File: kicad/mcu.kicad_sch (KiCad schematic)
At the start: 3 parts, among them J8 Conn_01x04, U5 ESP32-C6-DEVKITC-1-N8

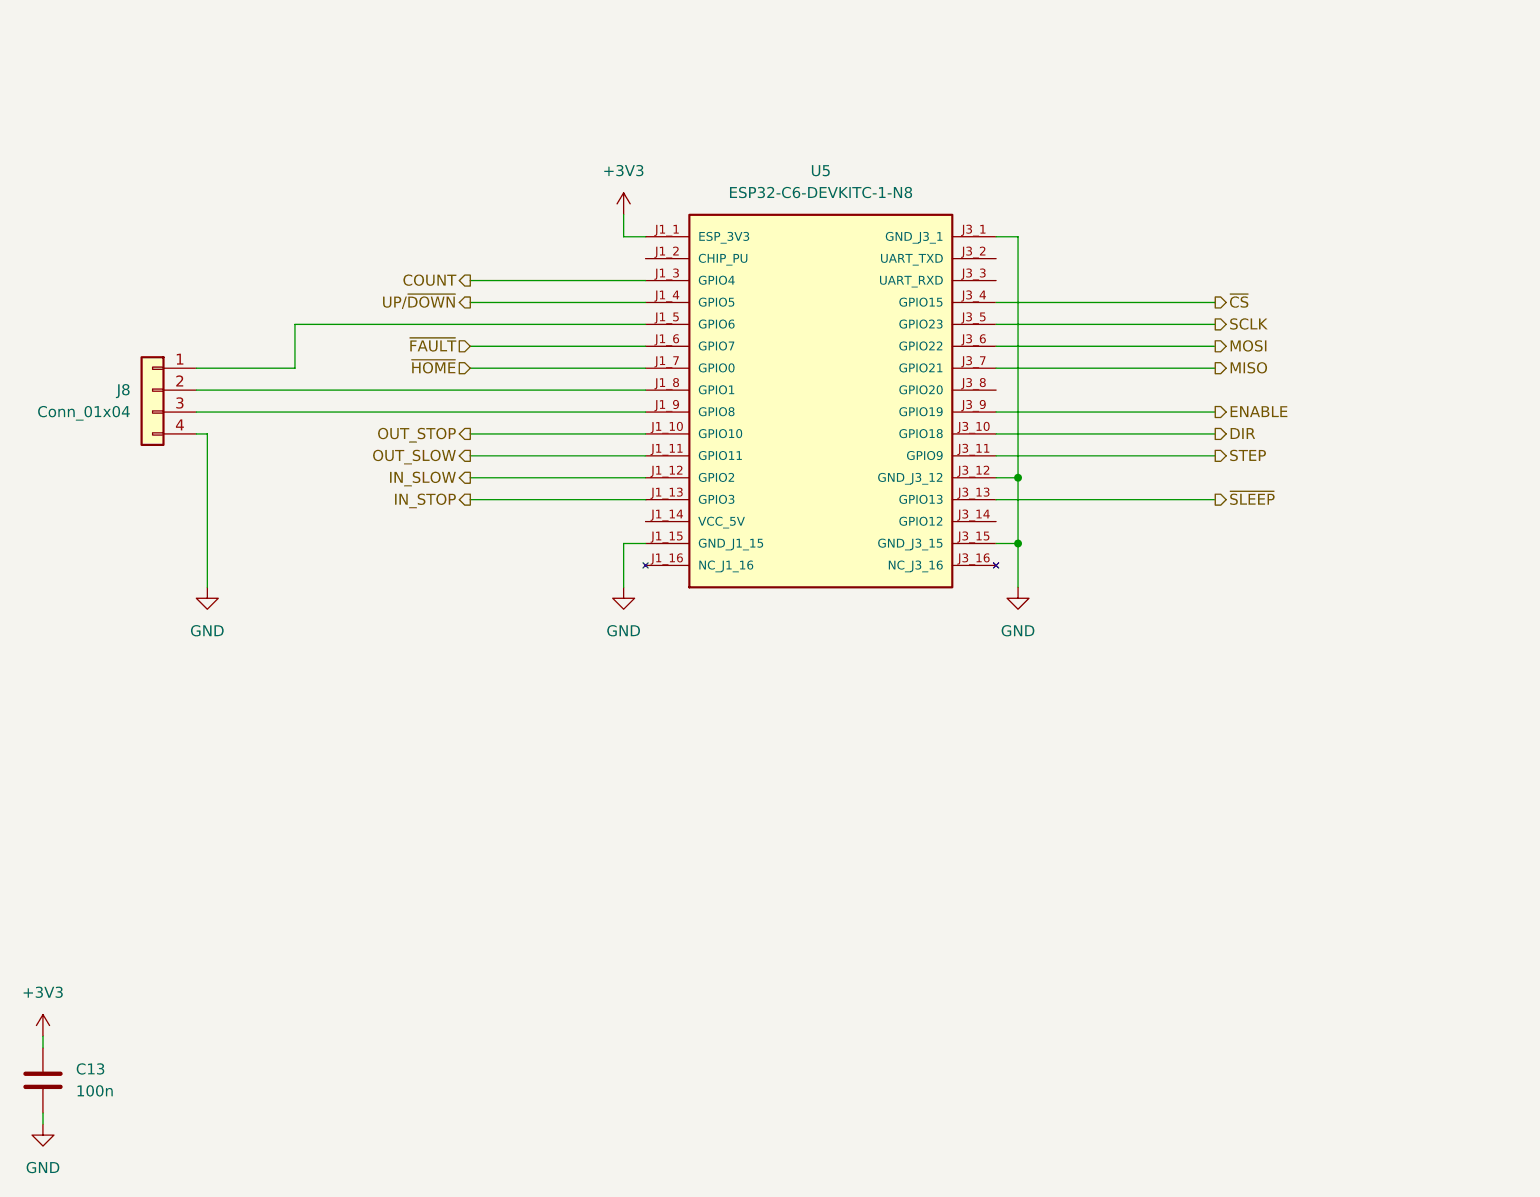
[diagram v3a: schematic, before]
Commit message: Finished the schematic and started the PCB.
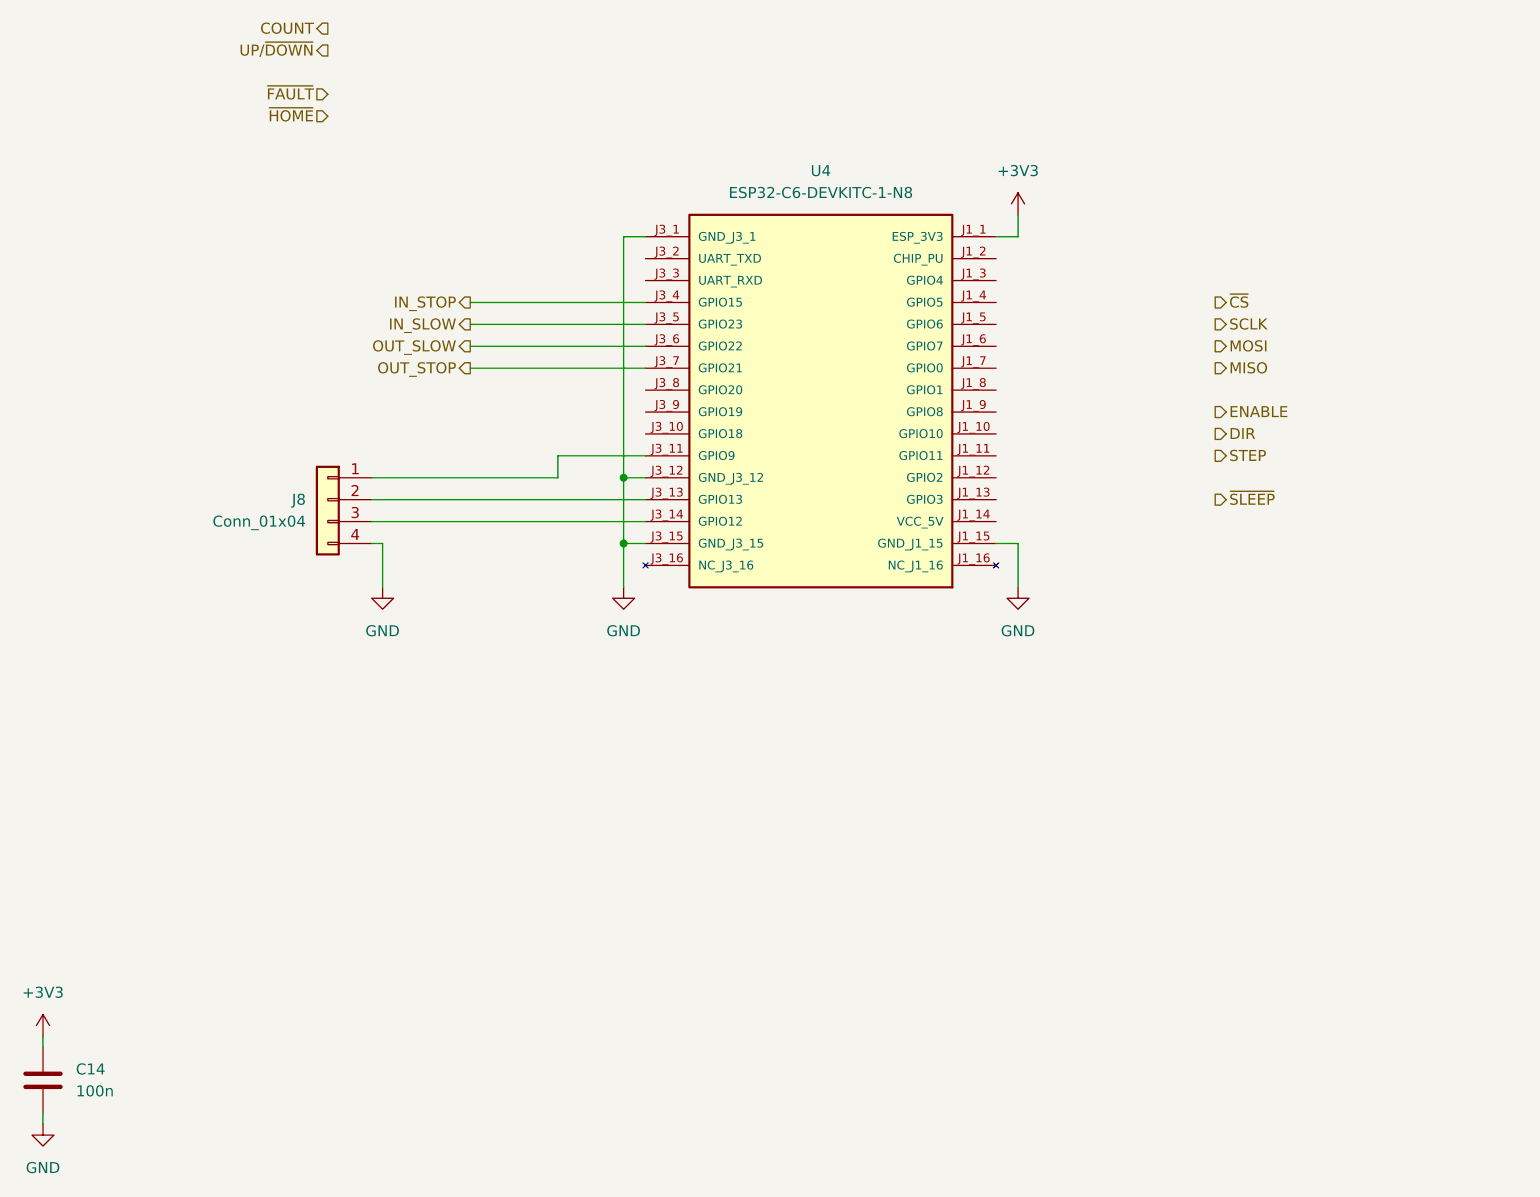
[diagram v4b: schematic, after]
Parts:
- renumbered C13 to C14, U5 to U4
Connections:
- net COUNT: no longer U4.J1_3 (GPIO4)
- net DIR: no longer U4.J3_10 (GPIO18)
- net ENABLE: no longer U4.J3_9 (GPIO19)
- net IN_SLOW: now also U4.J3_5 (GPIO23); no longer U4.J1_12 (GPIO2)
- net IN_STOP: now also U4.J3_4 (GPIO15); no longer U4.J1_13 (GPIO3)
- net MISO: no longer U4.J3_7 (GPIO21)
- net MOSI: no longer U4.J3_6 (GPIO22)
- net OUT_SLOW: now also U4.J3_6 (GPIO22); no longer U4.J1_11 (GPIO11)
- net OUT_STOP: now also U4.J3_7 (GPIO21); no longer U4.J1_10 (GPIO10)
- net SCLK: no longer U4.J3_5 (GPIO23)
- net STEP: no longer U4.J3_11 (GPIO9)
- net UP/~{DOWN}: no longer U4.J1_4 (GPIO5)
- net ~{CS}: no longer U4.J3_4 (GPIO15)
- net ~{FAULT}: no longer U4.J1_6 (GPIO7)
- net ~{HOME}: no longer U4.J1_7 (GPIO0)
- net ~{SLEEP}: no longer U4.J3_13 (GPIO13)
- net at J8.1 (Pin_1): now also U4.J3_11 (GPIO9); no longer U4.J1_5 (GPIO6)
- net at J8.2 (Pin_2): now also U4.J3_13 (GPIO13); no longer U4.J1_8 (GPIO1)
- net at J8.3 (Pin_3): now also U4.J3_14 (GPIO12); no longer U4.J1_9 (GPIO8)
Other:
- moved on the sheet: J8

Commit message: Completed the PCB design. Ready for final review.
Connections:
- net COUNT: now also U4.J1_2 (CHIP_PU)
- net DIR: now also U4.J1_7 (GPIO0)
- net ENABLE: now also U4.J1_6 (GPIO7)
- net MISO: now also U4.J1_11 (GPIO11)
- net MOSI: now also U4.J1_10 (GPIO10)
- net SCLK: now also U4.J1_9 (GPIO8)
- net STEP: now also U4.J1_8 (GPIO1)
- net UP/~{DOWN}: now also U4.J1_3 (GPIO4)
- net ~{CS}: now also U4.J1_12 (GPIO2)
- net ~{FAULT}: now also U4.J1_13 (GPIO3)
- net ~{SLEEP}: now also U4.J1_5 (GPIO6)
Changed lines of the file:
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@@
 	(title_block
 		(title "TV slider")
-		(date "2025-10-06")
-		(rev "1")
+		(date "2025-12-23")
+		(rev "1.0")
 		(company "NX Solutions")
 	)
@@
 	(wire
 		(pts
+			(xy 163.83 81.28) (xy 184.15 81.28)
+		)
+		(stroke
+			(width 0)
+			(type default)
+		)
+	)
+	(wire
+		(pts
+			(xy 163.83 99.06) (xy 184.15 99.06)
+		)
+		(stroke
+			(width 0)
+			(type default)
+		)
+	)
+	(wire
+		(pts
 			(xy 53.34 177.8) (xy 53.34 179.07)
 		)
@@
 	(wire
 		(pts
+			(xy 163.83 93.98) (xy 184.15 93.98)
+		)
+		(stroke
+			(width 0)
+			(type default)
+		)
+	)
+	(wire
+		(pts
 			(xy 91.44 109.22) (xy 123.19 109.22)
 		)
@@
 	(wire
 		(pts
+			(xy 163.83 101.6) (xy 184.15 101.6)
+		)
+		(stroke
+			(width 0)
+			(type default)
+		)
+	)
+	(wire
+		(pts
 			(xy 113.03 101.6) (xy 113.03 104.14)
 		)
@@
 	(wire
 		(pts
+			(xy 163.83 91.44) (xy 184.15 91.44)
+		)
+		(stroke
+			(width 0)
+			(type default)
+		)
+	)
+	(wire
+		(pts
+			(xy 163.83 86.36) (xy 184.15 86.36)
+		)
+		(stroke
+			(width 0)
+			(type default)
+		)
+	)
+	(wire
+		(pts
 			(xy 123.19 111.76) (xy 120.65 111.76)
 		)
@@
 	(wire
 		(pts
+			(xy 163.83 104.14) (xy 184.15 104.14)
+		)
+		(stroke
+			(width 0)
+			(type default)
+		)
+	)
+	(wire
+		(pts
 			(xy 163.83 111.76) (xy 166.37 111.76)
 		)
@@
 	(wire
 		(pts
+			(xy 163.83 96.52) (xy 184.15 96.52)
+		)
+		(stroke
+			(width 0)
+			(type default)
+		)
+	)
+	(wire
+		(pts
 			(xy 166.37 76.2) (xy 163.83 76.2)
 		)
@@
 	(wire
 		(pts
+			(xy 163.83 78.74) (xy 184.15 78.74)
+		)
+		(stroke
+			(width 0)
+			(type default)
+		)
+	)
+	(wire
+		(pts
+			(xy 163.83 106.68) (xy 184.15 106.68)
+		)
+		(stroke
+			(width 0)
+			(type default)
+		)
+	)
+	(wire
+		(pts
 			(xy 102.87 86.36) (xy 123.19 86.36)
 		)
@@
 		)
 	)
-	(hierarchical_label "~{HOME}"
-		(shape input)
-		(at 86.36 62.23 180)
-		(effects
-			(font
-				(size 1.27 1.27)
-			)
-			(justify right)
+	(wire
+		(pts
+			(xy 163.83 88.9) (xy 184.15 88.9)
+		)
+		(stroke
+			(width 0)
+			(type default)
 		)
 	)
 	(hierarchical_label "UP{slash}~{DOWN}"
 		(shape output)
-		(at 86.36 54.61 180)
-		(effects
-			(font
-				(size 1.27 1.27)
-			)
-			(justify right)
+		(at 184.15 81.28 0)
+		(effects
+			(font
+				(size 1.27 1.27)
+			)
+			(justify left)
 		)
 	)
 	(hierarchical_label "COUNT"
 		(shape output)
-		(at 86.36 52.07 180)
-		(effects
-			(font
-				(size 1.27 1.27)
-			)
-			(justify right)
+		(at 184.15 78.74 0)
+		(effects
+			(font
+				(size 1.27 1.27)
+			)
+			(justify left)
 		)
 	)
 	(hierarchical_label "SCLK"
 		(shape output)
-		(at 189.23 86.36 0)
+		(at 184.15 96.52 0)
 		(effects
 			(font
@@
 	(hierarchical_label "MOSI"
 		(shape output)
-		(at 189.23 88.9 0)
+		(at 184.15 99.06 0)
 		(effects
 			(font
@@
 	(hierarchical_label "MISO"
 		(shape output)
-		(at 189.23 91.44 0)
+		(at 184.15 101.6 0)
 		(effects
 			(font
@@
 	(hierarchical_label "~{FAULT}"
 		(shape input)
-		(at 86.36 59.69 180)
-		(effects
-			(font
-				(size 1.27 1.27)
-			)
-			(justify right)
+		(at 184.15 106.68 0)
+		(effects
+			(font
+				(size 1.27 1.27)
+			)
+			(justify left)
 		)
 	)
 	(hierarchical_label "~{CS}"
 		(shape output)
-		(at 189.23 83.82 0)
+		(at 184.15 104.14 0)
 		(effects
 			(font
@@
 	(hierarchical_label "ENABLE"
 		(shape output)
-		(at 189.23 96.52 0)
+		(at 184.15 88.9 0)
 		(effects
 			(font
@@
 	(hierarchical_label "STEP"
 		(shape output)
-		(at 189.23 101.6 0)
+		(at 184.15 93.98 0)
 		(effects
 			(font
@@
 	(hierarchical_label "DIR"
 		(shape output)
-		(at 189.23 99.06 0)
+		(at 184.15 91.44 0)
 		(effects
 			(font
@@
 	(hierarchical_label "~{SLEEP}"
 		(shape output)
-		(at 189.23 106.68 0)
-		(effects
-			(font
+		(at 184.15 86.36 0)
+		(effects
+			(font

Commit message: Reviewed the part numbers, footprints and pin numbers.
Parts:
- J8: MF (none) -> Wurth; MP (none) -> 61300411121; Supplier (none) -> Digi-Key; SupplierPN (none) -> 732-5317-ND
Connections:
- net COUNT: now also U4.J1_3 (GPIO4); no longer U4.J1_2 (CHIP_PU)
- net UP/~{DOWN}: now also U4.J1_4 (GPIO5); no longer U4.J1_3 (GPIO4)
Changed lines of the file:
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@@
+	(wire
+		(pts
+			(xy 163.83 99.06) (xy 184.15 99.06)
+		)
+		(stroke
+			(width 0)
+			(type default)
+		)
+	)
+	(wire
+		(pts
+			(xy 53.34 177.8) (xy 53.34 179.07)
+		)
+		(stroke
+			(width 0)
+			(type default)
+		)
+	)
 	(wire
 		(pts
@@
 	(wire
 		(pts
-			(xy 163.83 99.06) (xy 184.15 99.06)
-		)
-		(stroke
-			(width 0)
-			(type default)
-		)
-	)
-	(wire
-		(pts
-			(xy 53.34 177.8) (xy 53.34 179.07)
-		)
-		(stroke
-			(width 0)
-			(type default)
-		)
-	)
-	(wire
-		(pts
 			(xy 123.19 104.14) (xy 120.65 104.14)
 		)
@@
 	(wire
 		(pts
-			(xy 163.83 78.74) (xy 184.15 78.74)
+			(xy 163.83 83.82) (xy 184.15 83.82)
 		)
 		(stroke
@@
 		)
 	)
-	(hierarchical_label "UP{slash}~{DOWN}"
+	(hierarchical_label "COUNT"
 		(shape output)
 		(at 184.15 81.28 0)
-		(effects
-			(font
-				(size 1.27 1.27)
-			)
-			(justify left)
-		)
-	)
-	(hierarchical_label "COUNT"
-		(shape output)
-		(at 184.15 78.74 0)
 		(effects
 			(font
@@
 		(shape output)
 		(at 184.15 104.14 0)
+		(effects
+			(font
+				(size 1.27 1.27)
+			)
+			(justify left)
+		)
+	)
+	(hierarchical_label "UP{slash}~{DOWN}"
+		(shape output)
+		(at 184.15 83.82 0)
 		(effects
 			(font
@@
 			)
 		)
+		(property "SNAPEDA_PN" ""
+			(at 86.36 106.68 0)
+			(effects
+				(font
+					(size 1.27 1.27)
+				)
+				(hide yes)
+			)
+		)
+		(property "MF" "Wurth"
+			(at 86.36 106.68 0)
+			(effects
+				(font
+					(size 1.27 1.27)
+				)
+				(hide yes)
+			)
+		)
+		(property "MP" "61300411121"
+			(at 86.36 106.68 0)
+			(effects
+				(font
+					(size 1.27 1.27)
+				)
+				(hide yes)
+			)
+		)
+		(property "Supplier" "Digi-Key"
+			(at 86.36 106.68 0)
+			(effects
+				(font
+					(size 1.27 1.27)
+				)
+				(hide yes)
+			)
+		)
+		(property "SupplierPN" "732-5317-ND"
+			(at 86.36 106.68 0)
+			(effects
+				(font
+					(size 1.27 1.27)
+				)
+				(hide yes)
+			)
+		)
 		(pin "1"
 		)
@@
 		)
 		(property "MP" "GRM188R72A104KA35D"
+			(at 53.34 173.99 0)
+			(effects
+				(font
+					(size 1.27 1.27)
+				)
+				(hide yes)
+			)
+		)
+		(property "SNAPEDA_PN" ""
 			(at 53.34 173.99 0)
 			(effects
@@
 			(at 143.51 96.52 0)
 			(effects
+				(font
+					(size 1.27 1.27)
+				)
+				(hide yes)
+			)
+		)
+		(property "SNAPEDA_PN" ""
+			(at 143.51 96.52 0)
+			(effects

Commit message: Re-annotated and added extra capacitors for the 5V and 3V3 DC-DC converters. Added testpoints to the electronic fuse.
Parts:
- renumbered C14 to C16
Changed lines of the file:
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@@
 		(dnp no)
 		(fields_autoplaced yes)
-		(property "Reference" "#PWR032"
+		(property "Reference" "#PWR035"
 			(at 120.65 123.19 0)
 			(effects
@@
 			(project ""
 				(path "/914c4b67-a7a4-47f3-8515-668040fd3f8c/29d09a3f-5d85-4167-9532-6c777b8bdc81"
-					(reference "#PWR032")
+					(reference "#PWR035")
 					(unit 1)
 				)
@@
 		(dnp no)
 		(fields_autoplaced yes)
-		(property "Reference" "#PWR030"
+		(property "Reference" "#PWR034"
 			(at 92.71 123.19 0)
 			(effects
@@
 			(project "tv_slider"
 				(path "/914c4b67-a7a4-47f3-8515-668040fd3f8c/29d09a3f-5d85-4167-9532-6c777b8bdc81"
-					(reference "#PWR030")
+					(reference "#PWR034")
 					(unit 1)
 				)
@@
 		(dnp no)
 		(fields_autoplaced yes)
-		(property "Reference" "#PWR033"
+		(property "Reference" "#PWR037"
 			(at 53.34 172.72 0)
 			(effects
@@
 			(project "tv_slider"
 				(path "/914c4b67-a7a4-47f3-8515-668040fd3f8c/29d09a3f-5d85-4167-9532-6c777b8bdc81"
-					(reference "#PWR033")
+					(reference "#PWR037")
 					(unit 1)
 				)
@@
 		(dnp no)
 		(fields_autoplaced yes)
-		(property "Reference" "#PWR029"
+		(property "Reference" "#PWR033"
 			(at 166.37 77.47 0)
 			(effects
@@
 			(project ""
 				(path "/914c4b67-a7a4-47f3-8515-668040fd3f8c/29d09a3f-5d85-4167-9532-6c777b8bdc81"
-					(reference "#PWR029")
+					(reference "#PWR033")
 					(unit 1)
 				)
@@
 		(dnp no)
 		(fields_autoplaced yes)
-		(property "Reference" "#PWR031"
+		(property "Reference" "#PWR036"
 			(at 166.37 123.19 0)
 			(effects
@@
 			(project ""
 				(path "/914c4b67-a7a4-47f3-8515-668040fd3f8c/29d09a3f-5d85-4167-9532-6c777b8bdc81"
-					(reference "#PWR031")
+					(reference "#PWR036")
 					(unit 1)
 				)
@@
 		(dnp no)
 		(fields_autoplaced yes)
-		(property "Reference" "C14"
+		(property "Reference" "C16"
 			(at 57.15 172.7199 0)
 			(effects
@@
 			(project "tv_slider"
 				(path "/914c4b67-a7a4-47f3-8515-668040fd3f8c/29d09a3f-5d85-4167-9532-6c777b8bdc81"
-					(reference "C14")
+					(reference "C16")
 					(unit 1)
 				)
@@
 		(dnp no)
 		(fields_autoplaced yes)
-		(property "Reference" "#PWR034"
+		(property "Reference" "#PWR038"
 			(at 53.34 185.42 0)
 			(effects
@@
 			(project "tv_slider"
 				(path "/914c4b67-a7a4-47f3-8515-668040fd3f8c/29d09a3f-5d85-4167-9532-6c777b8bdc81"
-					(reference "#PWR034")
-					(unit 1)
-				)
+					(reference "#PWR038")
+					(unit 1)
+				)
